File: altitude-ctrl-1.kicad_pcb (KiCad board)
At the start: 2 copper layers, 90 x 90 mm, 93 parts, among them J1 Conn_01x02, J10 Conn_01x02, J11 Conn_01x04, J2 Conn_01x02, J3 Conn_01x05, J4 TC2030, J5 Conn_01x04_Pin, J6 Conn_01x02, J7 Conn_01x05, J8 Conn_01x05, J9 Conn_01x02, SW1 SW_Push, SW2 SW_SPST, SW3 SW_Push, SW4 SW_SPST, SW5 SW_Push, U1 HT753-1, U2 ULN2003A, U3 LM73100, U4 LM73100, U5 MAX6675, U6 STM32F103C8Tx, U7 SN65HVD230, Y1 8M

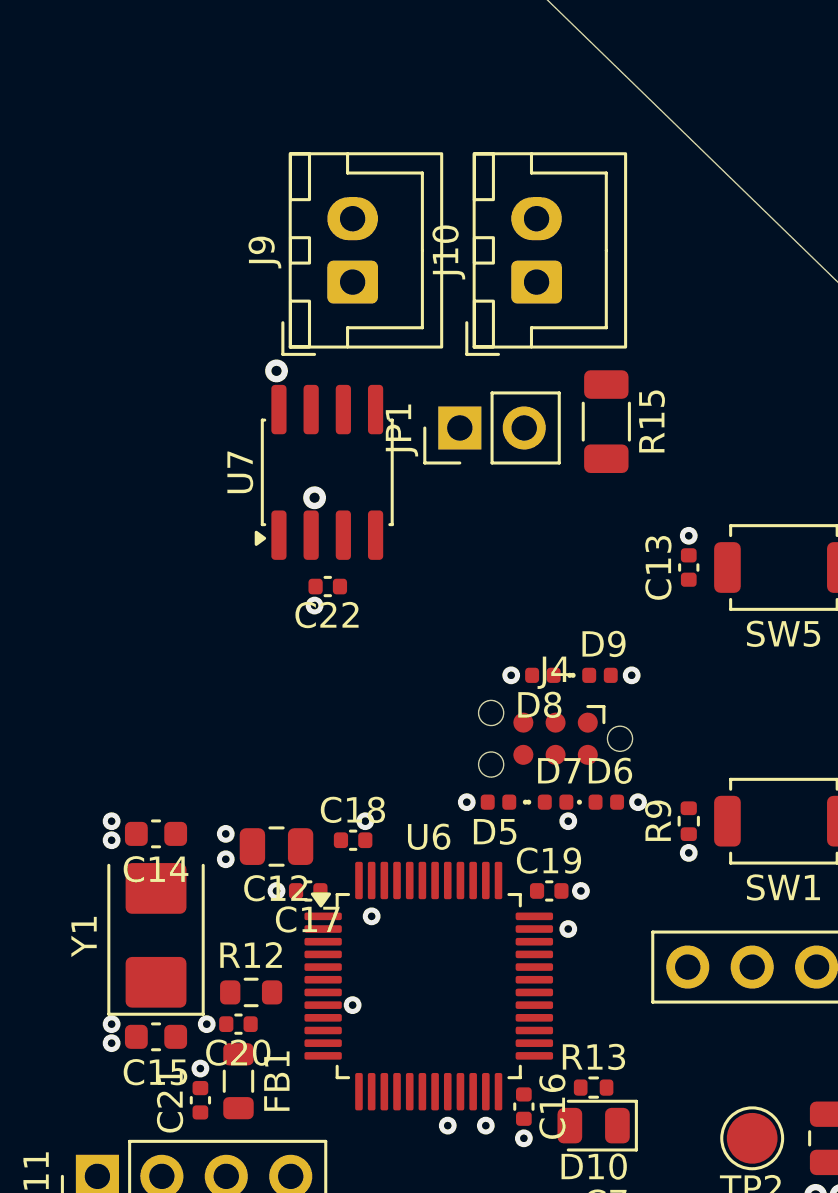
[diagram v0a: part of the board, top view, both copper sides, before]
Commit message: pcb: add xtal routing
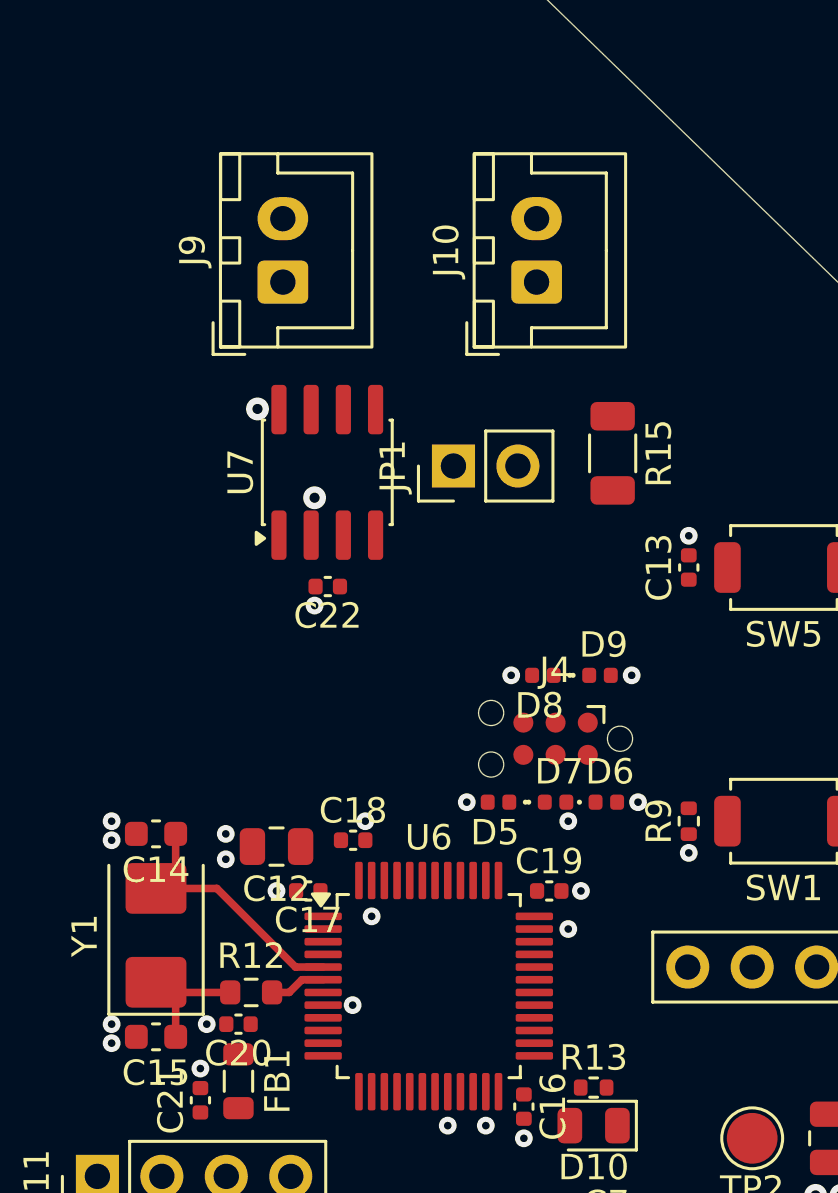
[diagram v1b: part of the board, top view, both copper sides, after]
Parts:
- moved J9 2.75 mm to (158.8, 58.8)
- moved JP1 1.52 mm to (165.5, 66.0)
- moved R15 1.27 mm to (171.8, 65.5)
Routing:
- net /XTAL_I: track 0.00 -> 10.3 mm
- net /XTAL_RO: track 0.00 -> 5.56 mm
- net /XTAL_O: track 0.00 -> 2.22 mm
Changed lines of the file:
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@@
 	(footprint "Resistor_SMD:R_1206_3216Metric"
 		(layer "F.Cu")
-		(at 171.5 64.25 -90)
+		(at 171.75 65.5 -90)
 		(descr "Resistor SMD 1206 (3216 Metric), square (rectangular) end terminal, IPC-7351 nominal, (Body size source: IPC-SM-782 page 72, https://www.pcb-3d.com/wordpress/wp-content/uploads/ipc-sm-782a_amendment_1_and_2.pdf)")
 		(tags "resistor")
@@
 	(footprint "Connector_PinHeader_2.54mm:PinHeader_1x02_P2.54mm_Vertical"
 		(layer "F.Cu")
-		(at 165.725 64.5 90)
+		(at 165.475 66 90)
 		(descr "Through hole straight pin header, 1x02, 2.54mm pitch, single row")
 		(tags "Through hole pin header THT 1x02 2.54mm single row")
@@
 	(footprint "Connector_JST:JST_XH_B2B-XH-A_1x02_P2.50mm_Vertical"
 		(layer "F.Cu")
-		(at 161.5 58.75 90)
+		(at 158.75 58.75 90)
 		(descr "JST XH series connector, B2B-XH-A (http://www.jst-mfg.com/product/pdf/eng/eXH.pdf)")
 		(tags "connector JST XH vertical")
@@
 	)
 	(via
-		(at 158.5 62.25)
+		(at 157.75 63.75)
 		(size 0.9)
 		(drill 0.4)
@@
 		(net "GND")
 	)
+	(segment
+		(start 154.15 86.75)
+		(end 153.75 86.35)
+		(width 0.3)
+		(layer "F.Cu")
+		(net "/XTAL_RO")
+	)
+	(segment
+		(start 154.525 88.5)
+		(end 154.525 87.125)
+		(width 0.3)
+		(layer "F.Cu")
+		(net "/XTAL_RO")
+	)
+	(segment
+		(start 154.525 87.125)
+		(end 153.75 86.35)
+		(width 0.3)
+		(layer "F.Cu")
+		(net "/XTAL_RO")
+	)
+	(segment
+		(start 156.675 86.75)
+		(end 154.15 86.75)
+		(width 0.3)
+		(layer "F.Cu")
+		(net "/XTAL_RO")
+	)
+	(segment
+		(start 159.5 86.25)
+		(end 160.3375 86.25)
+		(width 0.3)
+		(layer "F.Cu")
+		(net "/XTAL_O")
+	)
+	(segment
+		(start 159 86.75)
+		(end 159.5 86.25)
+		(width 0.3)
+		(layer "F.Cu")
+		(net "/XTAL_O")
+	)
+	(segment
+		(start 158.325 86.75)
+		(end 159 86.75)
+		(width 0.3)
+		(layer "F.Cu")
+		(net "/XTAL_O")
+	)
+	(segment
+		(start 156.15 82.65)
+		(end 153.75 82.65)
+		(width 0.3)
+		(layer "F.Cu")
+		(net "/XTAL_I")
+	)
+	(segment
+		(start 159.25 85.75)
+		(end 156.15 82.65)
+		(width 0.3)
+		(layer "F.Cu")
+		(net "/XTAL_I")
+	)
+	(segment
+		(start 154.525 81.875)
+		(end 153.75 82.65)
+		(width 0.3)
+		(layer "F.Cu")
+		(net "/XTAL_I")
+	)
+	(segment
+		(start 160.3375 85.75)
+		(end 159.25 85.75)
+		(width 0.3)
+		(layer "F.Cu")
+		(net "/XTAL_I")
+	)
+	(segment
+		(start 154.525 80.5)
+		(end 154.525 81.875)
+		(width 0.3)
+		(layer "F.Cu")
+		(net "/XTAL_I")
+	)
 	(zone

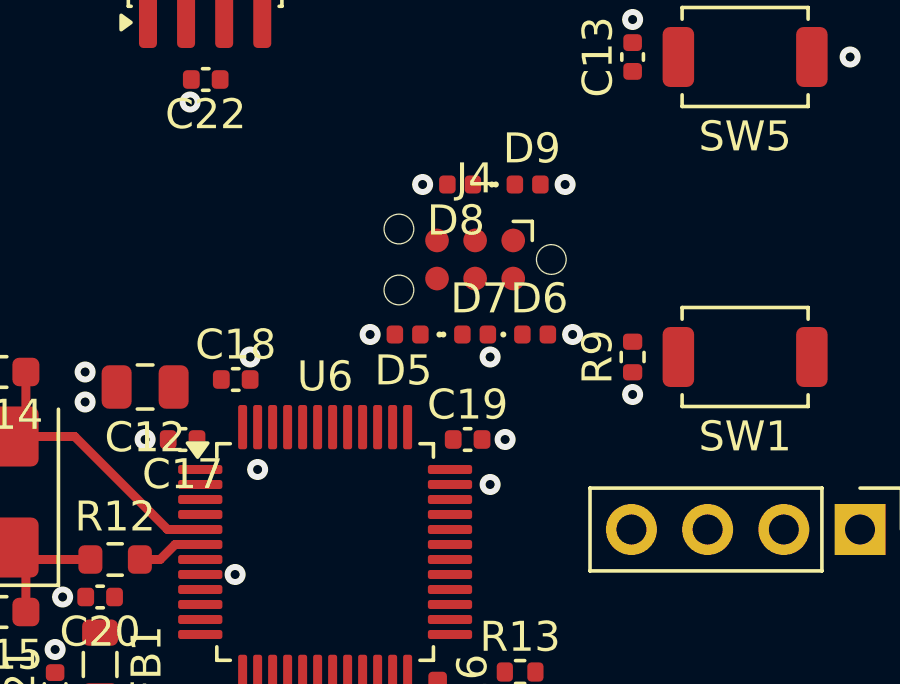
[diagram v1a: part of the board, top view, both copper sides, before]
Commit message: pcb: add swd routing
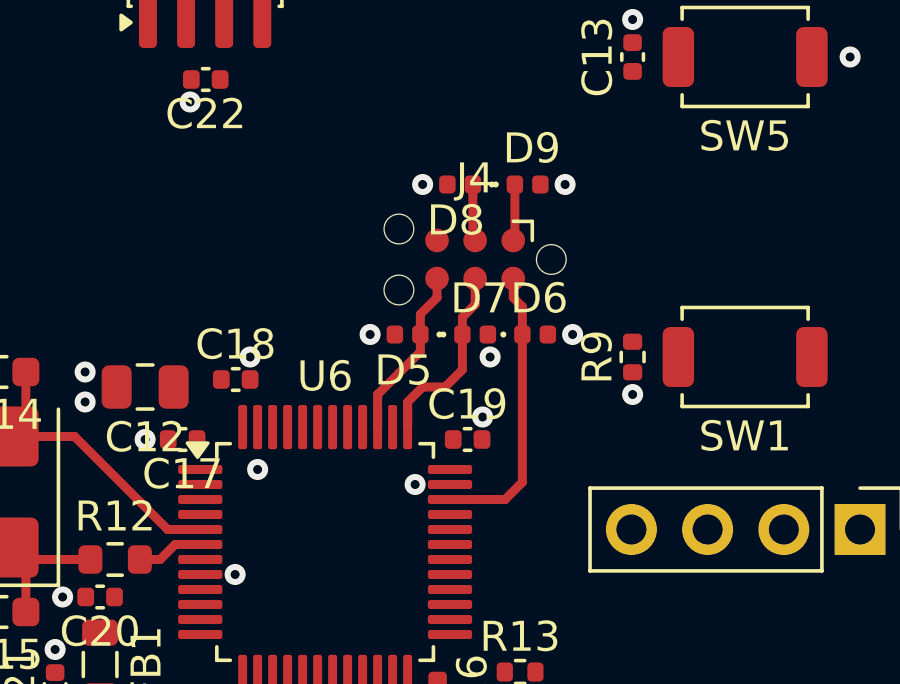
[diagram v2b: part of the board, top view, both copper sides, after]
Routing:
- net /SWDIO: track 0.00 -> 9.57 mm
- net /SWCLK: track 0.00 -> 6.32 mm
- net /SWO: track 0.00 -> 5.77 mm
- net /NRST: track 0.00 -> 1.90 mm
- net +3V3: track 0.00 -> 1.89 mm
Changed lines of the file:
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@@
 	)
 	(via
-		(at 170.5 82.75)
+		(at 169.75 82)
 		(size 0.7)
 		(drill 0.3)
@@
 	)
 	(via
-		(at 170 84.25)
+		(at 167.5 84.25)
 		(size 0.7)
 		(drill 0.3)
@@
 	)
 	(segment
+		(start 170.825 76.06)
+		(end 170.77 76.115)
+		(width 0.3)
+		(layer "F.Cu")
+		(net "+3V3")
+	)
+	(segment
+		(start 170.825 74.25)
+		(end 170.825 76.06)
+		(width 0.3)
+		(layer "F.Cu")
+		(net "+3V3")
+	)
+	(segment
+		(start 170.77 78.02)
+		(end 171.075 78.325)
+		(width 0.3)
+		(layer "F.Cu")
+		(net "/SWDIO")
+	)
+	(segment
+		(start 171.075 78.325)
+		(end 171.075 79.25)
+		(width 0.3)
+		(layer "F.Cu")
+		(net "/SWDIO")
+	)
+	(segment
+		(start 170.5 84.75)
+		(end 171.075 84.175)
+		(width 0.3)
+		(layer "F.Cu")
+		(net "/SWDIO")
+	)
+	(segment
+		(start 171.075 84.175)
+		(end 171.075 79.25)
+		(width 0.3)
+		(layer "F.Cu")
+		(net "/SWDIO")
+	)
+	(segment
+		(start 168.6625 84.75)
+		(end 170.5 84.75)
+		(width 0.3)
+		(layer "F.Cu")
+		(net "/SWDIO")
+	)
+	(segment
+		(start 170.77 77.385)
+		(end 170.77 78.02)
+		(width 0.3)
+		(layer "F.Cu")
+		(net "/SWDIO")
+	)
+	(segment
+		(start 169.425 74.25)
+		(end 169.425 76.04)
+		(width 0.3)
+		(layer "F.Cu")
+		(net "/NRST")
+	)
+	(segment
+		(start 169.425 76.04)
+		(end 169.5 76.115)
+		(width 0.3)
+		(layer "F.Cu")
+		(net "/NRST")
+	)
+	(segment
+		(start 169.075 78.675)
+		(end 169.5 78.25)
+		(width 0.3)
+		(layer "F.Cu")
+		(net "/SWCLK")
+	)
+	(segment
+		(start 169.075 79.25)
+		(end 169.075 78.675)
+		(width 0.3)
+		(layer "F.Cu")
+		(net "/SWCLK")
+	)
+	(segment
+		(start 168.5 81)
+		(end 169.075 80.425)
+		(width 0.3)
+		(layer "F.Cu")
+		(net "/SWCLK")
+	)
+	(segment
+		(start 169.075 80.425)
+		(end 169.075 79.25)
+		(width 0.3)
+		(layer "F.Cu")
+		(net "/SWCLK")
+	)
+	(segment
+		(start 169.5 78.25)
+		(end 169.5 77.385)
+		(width 0.3)
+		(layer "F.Cu")
+		(net "/SWCLK")
+	)
+	(segment
+		(start 167.75 81)
+		(end 168.5 81)
+		(width 0.3)
+		(layer "F.Cu")
+		(net "/SWCLK")
+	)
+	(segment
+		(start 167.25 81.5)
+		(end 167.75 81)
+		(width 0.3)
+		(layer "F.Cu")
+		(net "/SWCLK")
+	)
+	(segment
+		(start 167.25 82.3375)
+		(end 167.25 81.5)
+		(width 0.3)
+		(layer "F.Cu")
+		(net "/SWCLK")
+	)
+	(segment
+		(start 167.675 78.575)
+		(end 167.675 79.25)
+		(width 0.3)
+		(layer "F.Cu")
+		(net "/SWO")
+	)
+	(segment
+		(start 168.23 78.02)
+		(end 167.675 78.575)
+		(width 0.3)
+		(layer "F.Cu")
+		(net "/SWO")
+	)
+	(segment
+		(start 168.23 77.385)
+		(end 168.23 78.02)
+		(width 0.3)
+		(layer "F.Cu")
+		(net "/SWO")
+	)
+	(segment
+		(start 166.25 81.25)
+		(end 167.675 79.825)
+		(width 0.3)
+		(layer "F.Cu")
+		(net "/SWO")
+	)
+	(segment
+		(start 166.25 82.3375)
+		(end 166.25 81.25)
+		(width 0.3)
+		(layer "F.Cu")
+		(net "/SWO")
+	)
+	(segment
+		(start 167.675 79.825)
+		(end 167.675 79.25)
+		(width 0.3)
+		(layer "F.Cu")
+		(net "/SWO")
+	)
+	(segment

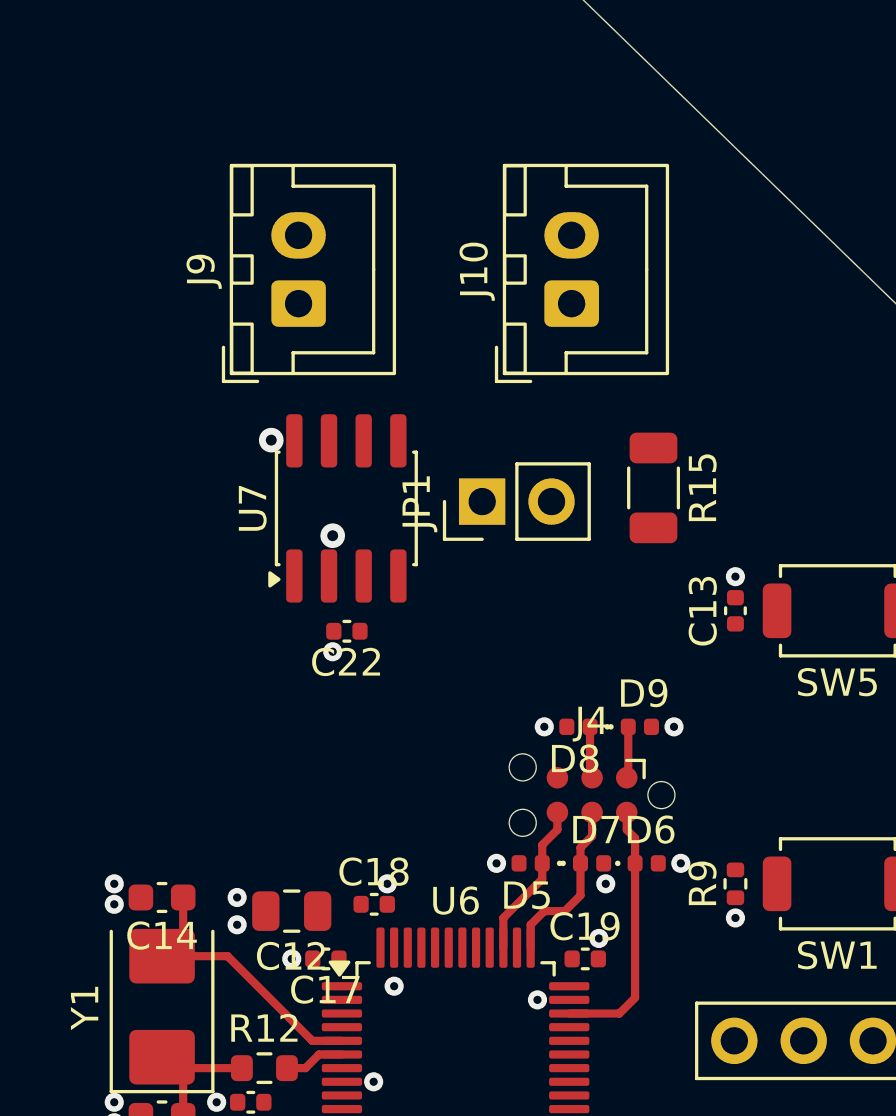
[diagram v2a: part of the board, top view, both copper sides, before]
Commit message: pcb: add can routing
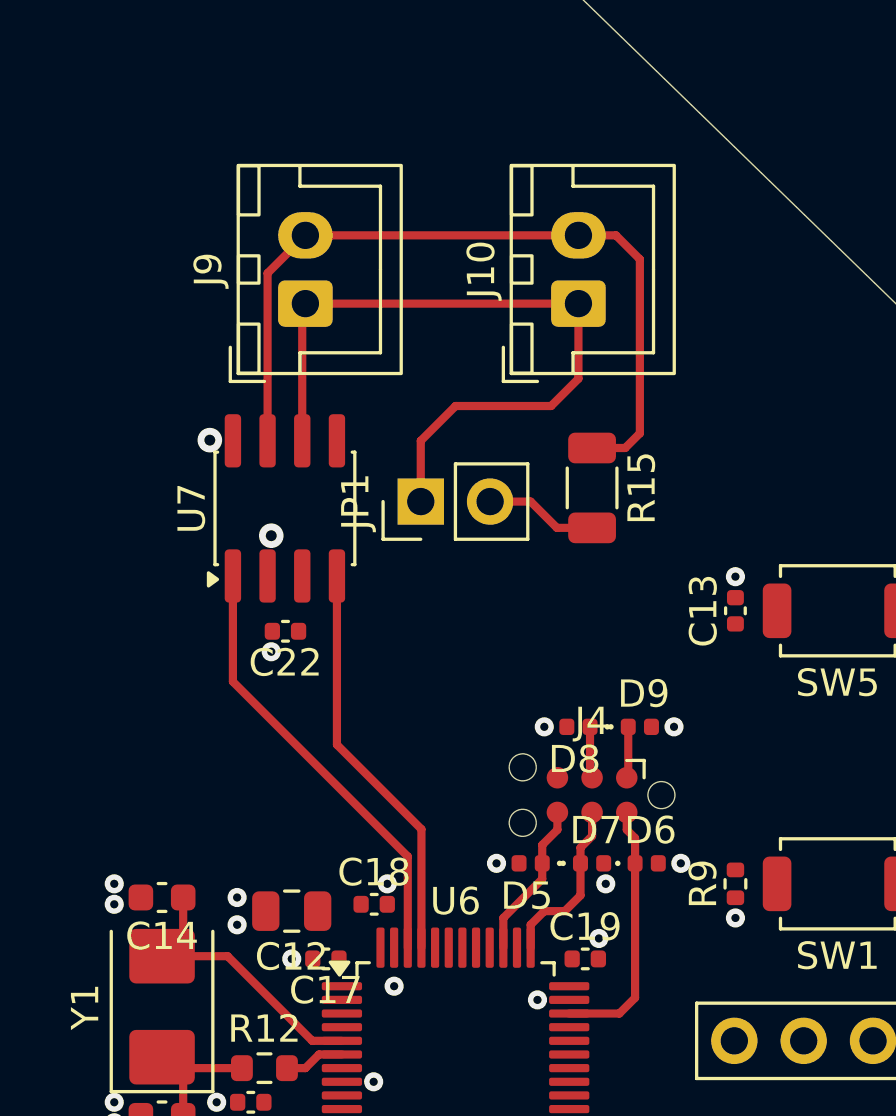
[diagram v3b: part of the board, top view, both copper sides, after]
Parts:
- moved C22 2.25 mm to (158.3, 70.8)
- moved JP1 2.25 mm to (163.2, 66.0)
- moved R15 2.25 mm to (169.5, 65.5)
- moved U7 2.25 mm to (158.2, 66.2)
- moved J10 0.25 mm to (169.0, 58.8)
- moved J9 0.25 mm to (159.0, 58.8)
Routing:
- net /CANH: track 0.00 -> 29.1 mm
- net /CANL: track 0.00 -> 26.8 mm
- net /CAN_TX: track 0.00 -> 16.3 mm
- net /CAN_RX: track 0.00 -> 14.9 mm
- net Net-(JP1-B): track 0.00 -> 4.13 mm
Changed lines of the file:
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@@
 	(footprint "Resistor_SMD:R_1206_3216Metric"
 		(layer "F.Cu")
-		(at 171.75 65.5 -90)
+		(at 169.5 65.5 -90)
 		(descr "Resistor SMD 1206 (3216 Metric), square (rectangular) end terminal, IPC-7351 nominal, (Body size source: IPC-SM-782 page 72, https://www.pcb-3d.com/wordpress/wp-content/uploads/ipc-sm-782a_amendment_1_and_2.pdf)")
 		(tags "resistor")
@@
 	(footprint "Package_SO:SOIC-8_3.9x4.9mm_P1.27mm"
 		(layer "F.Cu")
-		(at 160.5 66.25 90)
+		(at 158.25 66.25 90)
 		(descr "SOIC, 8 Pin (JEDEC MS-012AA, https://www.analog.com/media/en/package-pcb-resources/package/pkg_pdf/soic_narrow-r/r_8.pdf)")
 		(tags "SOIC SO")
@@
 	(footprint "Connector_PinHeader_2.54mm:PinHeader_1x02_P2.54mm_Vertical"
 		(layer "F.Cu")
-		(at 165.475 66 90)
+		(at 163.225 66 90)
 		(descr "Through hole straight pin header, 1x02, 2.54mm pitch, single row")
 		(tags "Through hole pin header THT 1x02 2.54mm single row")
@@
 	(footprint "Connector_JST:JST_XH_B2B-XH-A_1x02_P2.50mm_Vertical"
 		(layer "F.Cu")
-		(at 168.75 58.75 90)
+		(at 169 58.75 90)
 		(descr "JST XH series connector, B2B-XH-A (http://www.jst-mfg.com/product/pdf/eng/eXH.pdf)")
 		(tags "connector JST XH vertical")
@@
 	(footprint "Connector_JST:JST_XH_B2B-XH-A_1x02_P2.50mm_Vertical"
 		(layer "F.Cu")
-		(at 158.75 58.75 90)
+		(at 159 58.75 90)
 		(descr "JST XH series connector, B2B-XH-A (http://www.jst-mfg.com/product/pdf/eng/eXH.pdf)")
 		(tags "connector JST XH vertical")
@@
 	(footprint "Capacitor_SMD:C_0402_1005Metric"
 		(layer "F.Cu")
-		(at 160.52 70.75 180)
+		(at 158.27 70.75 180)
 		(descr "Capacitor SMD 0402 (1005 Metric), square (rectangular) end terminal, IPC-7351 nominal, (Body size source: IPC-SM-782 page 76, https://www.pcb-3d.com/wordpress/wp-content/uploads/ipc-sm-782a_amendment_1_and_2.pdf)")
 		(tags "capacitor")
@@
 	)
 	(via
-		(at 160 67.25)
+		(at 157.75 67.25)
 		(size 0.9)
 		(drill 0.4)
@@
 	)
 	(via
-		(at 160 71.5)
+		(at 157.75 71.5)
 		(size 0.7)
 		(drill 0.3)
@@
 	)
 	(via
-		(at 157.75 63.75)
+		(at 155.5 63.75)
 		(size 0.9)
 		(drill 0.4)
@@
 		(net "/XTAL_I")
 	)
+	(segment
+		(start 163.25 78)
+		(end 160.155 74.905)
+		(width 0.3)
+		(layer "F.Cu")
+		(net "/CAN_RX")
+	)
+	(segment
+		(start 160.155 74.905)
+		(end 160.155 68.725)
+		(width 0.3)
+		(layer "F.Cu")
+		(net "/CAN_RX")
+	)
+	(segment
+		(start 163.25 82.3375)
+		(end 163.25 78)
+		(width 0.3)
+		(layer "F.Cu")
+		(net "/CAN_RX")
+	)
+	(segment
+		(start 162.75 82.3375)
+		(end 162.75 79)
+		(width 0.3)
+		(layer "F.Cu")
+		(net "/CAN_TX")
+	)
+	(segment
+		(start 156.345 72.595)
+		(end 156.345 68.725)
+		(width 0.3)
+		(layer "F.Cu")
+		(net "/CAN_TX")
+	)
+	(segment
+		(start 162.75 79)
+		(end 156.345 72.595)
+		(width 0.3)
+		(layer "F.Cu")
+		(net "/CAN_TX")
+	)
+	(segment
+		(start 170.7125 64.0375)
+		(end 171.25 63.5)
+		(width 0.3)
+		(layer "F.Cu")
+		(net "/CANH")
+	)
+	(segment
+		(start 171.25 57.125)
+		(end 170.375 56.25)
+		(width 0.3)
+		(layer "F.Cu")
+		(net "/CANH")
+	)
+	(segment
+		(start 169.5 64.0375)
+		(end 170.7125 64.0375)
+		(width 0.3)
+		(layer "F.Cu")
+		(net "/CANH")
+	)
+	(segment
+		(start 157.615 57.635)
+		(end 159 56.25)
+		(width 0.3)
+		(layer "F.Cu")
+		(net "/CANH")
+	)
+	(segment
+		(start 171.25 63.5)
+		(end 171.25 57.125)
+		(width 0.3)
+		(layer "F.Cu")
+		(net "/CANH")
+	)
+	(segment
+		(start 157.615 63.775)
+		(end 157.615 57.635)
+		(width 0.3)
+		(layer "F.Cu")
+		(net "/CANH")
+	)
+	(segment
+		(start 170.375 56.25)
+		(end 169 56.25)
+		(width 0.3)
+		(layer "F.Cu")
+		(net "/CANH")
+	)
+	(segment
+		(start 169 56.25)
+		(end 159 56.25)
+		(width 0.3)
+		(layer "F.Cu")
+		(net "/CANH")
+	)
+	(segment
+		(start 165.765 66)
+		(end 167.25 66)
+		(width 0.3)
+		(layer "F.Cu")
+		(net "Net-(JP1-B)")
+	)
+	(segment
+		(start 168.2125 66.9625)
+		(end 169.5 66.9625)
+		(width 0.3)
+		(layer "F.Cu")
+		(net "Net-(JP1-B)")
+	)
+	(segment
+		(start 167.25 66)
+		(end 168.2125 66.9625)
+		(width 0.3)
+		(layer "F.Cu")
+		(net "Net-(JP1-B)")
+	)
+	(segment
+		(start 158.885 58.865)
+		(end 159 58.75)
+		(width 0.3)
+		(layer "F.Cu")
+		(net "/CANL")
+	)
+	(segment
+		(start 169 61.5)
+		(end 169 58.75)
+		(width 0.3)
+		(layer "F.Cu")
+		(net "/CANL")
+	)
+	(segment
+		(start 163.225 66)
+		(end 163.225 63.775)
+		(width 0.3)
+		(layer "F.Cu")
+		(net "/CANL")
+	)
+	(segment
+		(start 163.225 63.775)
+		(end 164.5 62.5)
+		(width 0.3)
+		(layer "F.Cu")
+		(net "/CANL")
+	)
+	(segment
+		(start 159 58.75)
+		(end 169 58.75)
+		(width 0.3)
+		(layer "F.Cu")
+		(net "/CANL")
+	)
+	(segment
+		(start 168 62.5)
+		(end 169 61.5)
+		(width 0.3)
+		(layer "F.Cu")
+		(net "/CANL")
+	)
+	(segment
+		(start 158.885 63.775)
+		(end 158.885 58.865)
+		(width 0.3)
+		(layer "F.Cu")
+		(net "/CANL")
+	)
+	(segment
+		(start 164.5 62.5)
+		(end 168 62.5)
+		(width 0.3)
+		(layer "F.Cu")
+		(net "/CANL")
+	)
 	(zone
